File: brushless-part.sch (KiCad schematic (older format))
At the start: 13 parts, among them K1 Maxon-200142, K2 Maxon-200142, U2 DEC24/2, U3 DEC24/2

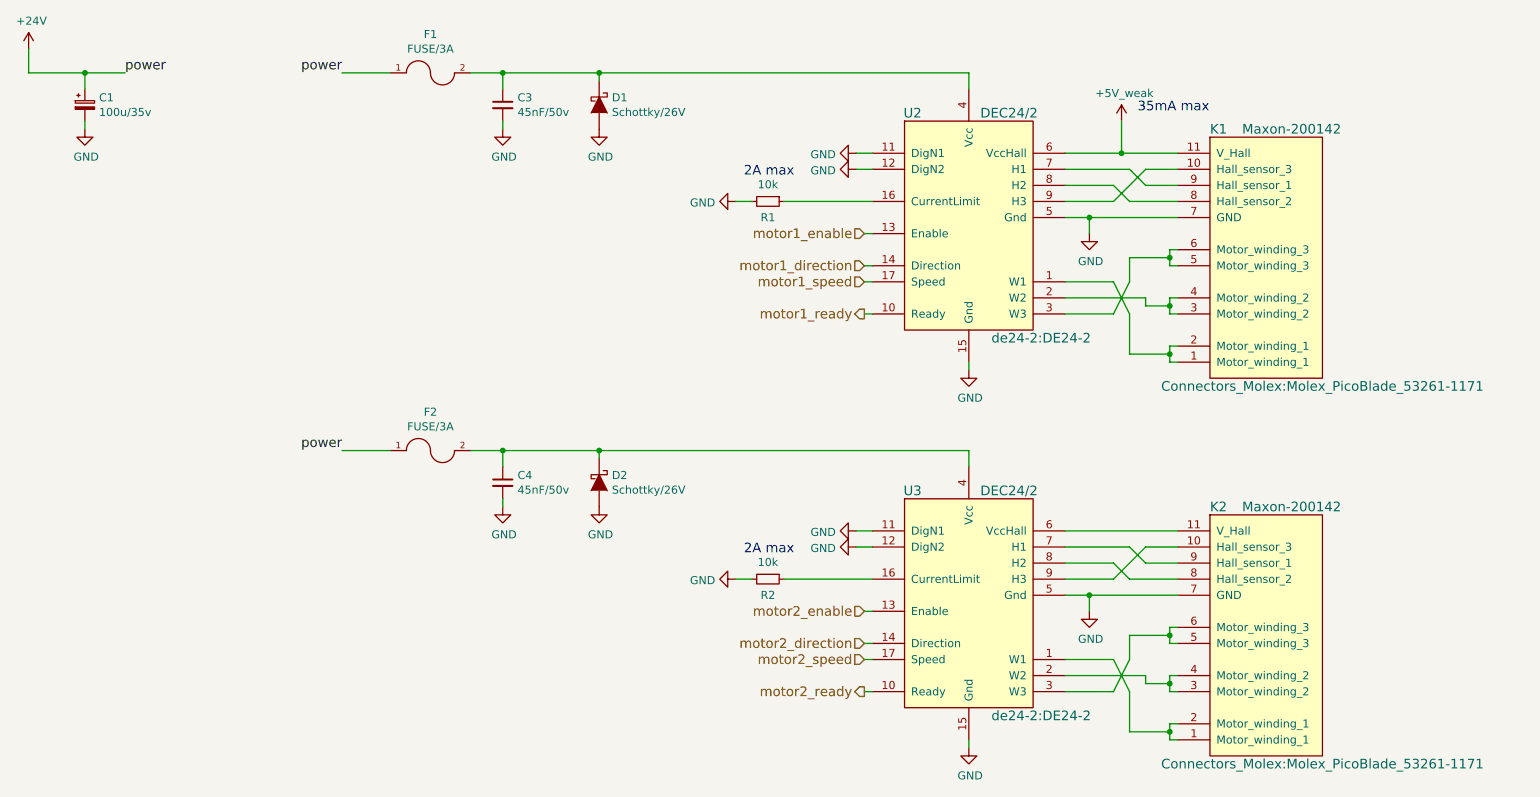
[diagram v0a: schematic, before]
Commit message: schematic seems ok, ongoing routing
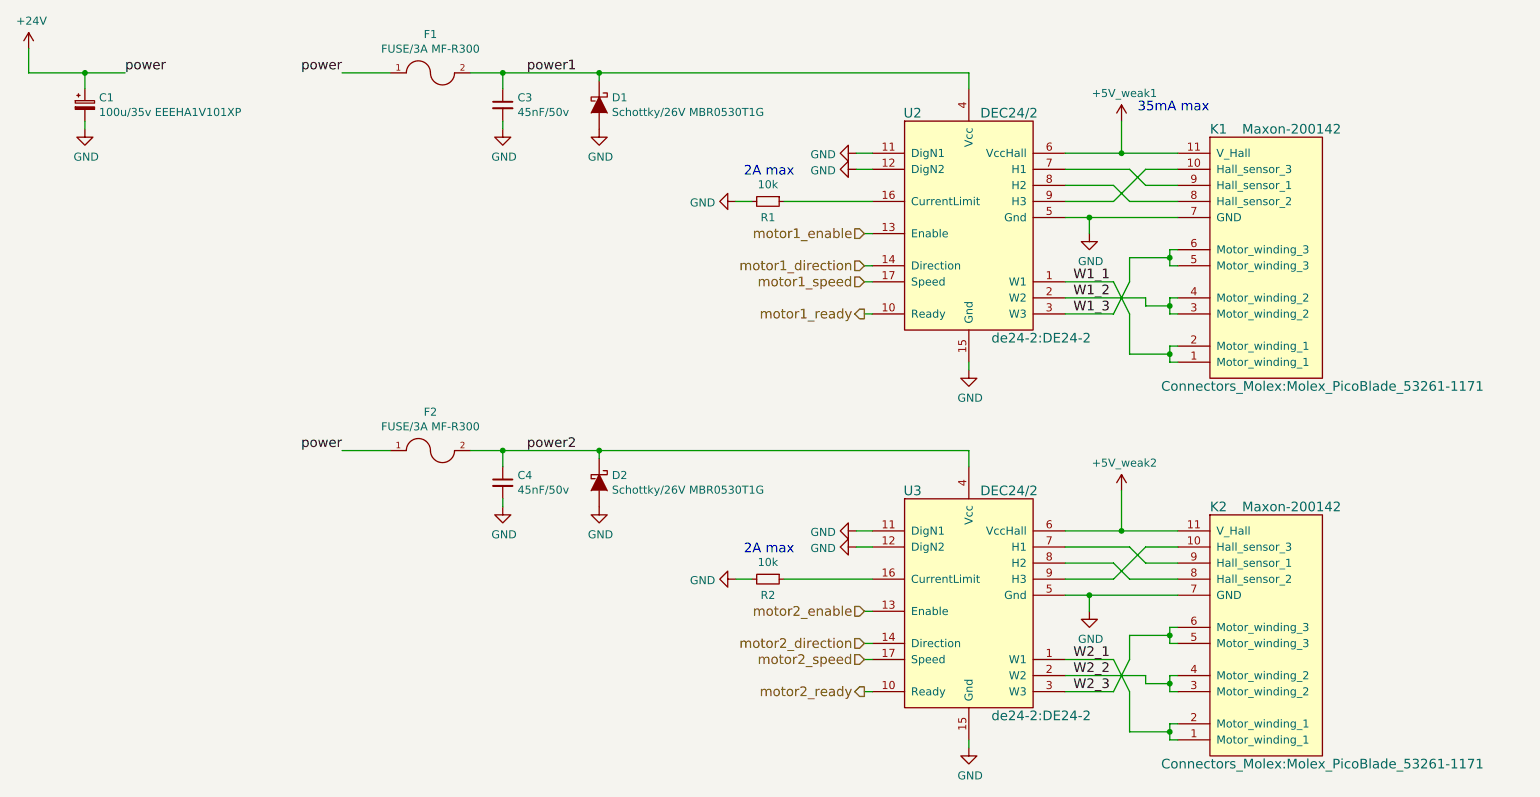
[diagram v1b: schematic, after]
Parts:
- C1: value 100u/35v -> 100u/35v EEEHA1V101XP; footprint Capacitors_ThroughHole:C_Radial_D10_L13_P5 -> Capacitors_SMD:c_elec_6.3x4.5
- C3, C4: footprint Capacitors_SMD:C_1210 -> Capacitors_SMD:C_0805
- D1, D2: value Schottky/26V -> Schottky/26V MBR0530T1G; footprint Diodes_SMD:DO-214AB -> Diodes_SMD:SOD-123
- F1: value FUSE/3A -> FUSE/3A MF-R300; footprint Fuse_Holders_and_Fuses:Fuse_SMD2920 -> Fuse_Holders_and_Fuses:Fuse_TE5_Littlefuse-395Series
- F2: value FUSE/3A -> FUSE/3A MF-R300
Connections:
- net W1_1: now reaches K1.1 (Motor_winding_1), K1.2 (Motor_winding_1), U2.1 (W1)
- net W1_2: now reaches K1.3 (Motor_winding_2), K1.4 (Motor_winding_2), U2.2 (W2)
- net W1_3: now reaches K1.5 (Motor_winding_3), K1.6 (Motor_winding_3), U2.3 (W3)
- net power1: now reaches C3.1, D1.1 (K), F1.2, U2.4 (Vcc)
- net W2_1: now reaches K2.1 (Motor_winding_1), K2.2 (Motor_winding_1), U3.1 (W1)
- net W2_2: now reaches K2.3 (Motor_winding_2), K2.4 (Motor_winding_2), U3.2 (W2)
- net W2_3: now reaches K2.5 (Motor_winding_3), K2.6 (Motor_winding_3), U3.3 (W3)
- net power2: now reaches C4.1, D2.1 (K), F2.2, U3.4 (Vcc)
- net +5V_weak2: now reaches K2.11 (V_Hall), U3.6 (VccHall)
- net +5V_weak renamed +5V_weak1
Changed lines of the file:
@@
 $Descr A4 11693 8268
 encoding utf-8
-Sheet 2 7
+Sheet 2 9
 Title "Brushless glue"
 Date "2016-04-02"
@@
 $EndComp
 $Comp
-L GND #PWR01
+L GND #PWR13
 U 1 1 570025FB
 P 7300 3700
-F 0 "#PWR01" H 7300 3450 50  0001 C CNN
+F 0 "#PWR13" H 7300 3450 50  0001 C CNN
 F 1 "GND" H 7308 3527 50  0000 C CNN
 F 2 "" H 7300 3700 50  0000 C CNN
@@
 $EndComp
 $Comp
-L GND #PWR02
+L GND #PWR15
 U 1 1 570025FD
 P 8050 2850
-F 0 "#PWR02" H 8050 2600 50  0001 C CNN
+F 0 "#PWR15" H 8050 2600 50  0001 C CNN
 F 1 "GND" H 8058 2677 50  0000 C CNN
 F 2 "" H 8050 2850 50  0000 C CNN
@@
 $EndComp
 $Comp
-L GND #PWR03
+L GND #PWR9
 U 1 1 570025FE
 P 6600 2350
-F 0 "#PWR03" H 6600 2100 50  0001 C CNN
+F 0 "#PWR9" H 6600 2100 50  0001 C CNN
 F 1 "GND" V 6608 2222 50  0000 R CNN
 F 2 "" H 6600 2350 50  0000 C CNN
@@
 $EndComp
 $Comp
-L GND #PWR04
+L GND #PWR10
 U 1 1 570025FF
 P 6600 2450
-F 0 "#PWR04" H 6600 2200 50  0001 C CNN
+F 0 "#PWR10" H 6600 2200 50  0001 C CNN
 F 1 "GND" V 6608 2322 50  0000 R CNN
 F 2 "" H 6600 2450 50  0000 C CNN
@@
 P 3950 1850
 F 0 "F1" H 3950 2090 50  0000 C CNN
-F 1 "FUSE/3A" H 3950 1999 50  0000 C CNN
-F 2 "Fuse_Holders_and_Fuses:Fuse_SMD2920" H 3950 1850 50  0001 C CNN
+F 1 "FUSE/3A MF-R300" H 3950 1999 50  0000 C CNN
+F 2 "Fuse_Holders_and_Fuses:Fuse_TE5_Littlefuse-395Series" H 3950 1850 50  0001 C CNN
 F 3 "" H 3950 1850 50  0000 C CNN
 	1    3950 1850
@@
 F 0 "C3" H 4492 2096 50  0000 L CNN
 F 1 "45nF/50v" H 4492 2005 50  0000 L CNN
-F 2 "Capacitors_SMD:C_1210" H 4400 2050 50  0001 C CNN
+F 2 "Capacitors_SMD:C_0805" H 4400 2050 50  0001 C CNN
 F 3 "" H 4400 2050 50  0000 C CNN
 	1    4400 2050
@@
 P 5000 2050
 F 0 "D1" V 4954 2129 50  0000 L CNN
-F 1 "Schottky/26V" V 5045 2129 50  0000 L CNN
-F 2 "Diodes_SMD:DO-214AB" H 5000 2050 50  0001 C CNN
-F 3 "" H 5000 2050 50  0000 C CNN
+F 1 "Schottky/26V MBR0530T1G" V 5045 2129 50  0000 L CNN
+F 2 "Diodes_SMD:SOD-123" H 5000 2050 50  0001 C CNN
+F 3 "http://www.farnell.com/datasheets/85890.pdf" H 5000 2050 50  0001 C CNN
 	1    5000 2050
 	0    1    1    0
 $EndComp
 $Comp
-L GND #PWR05
+L GND #PWR5
 U 1 1 57003EB2
 P 5000 2200
-F 0 "#PWR05" H 5000 1950 50  0001 C CNN
+F 0 "#PWR5" H 5000 1950 50  0001 C CNN
 F 1 "GND" H 5008 2027 50  0000 C CNN
 F 2 "" H 5000 2200 50  0000 C CNN
@@
 $EndComp
 $Comp
-L GND #PWR06
+L GND #PWR3
 U 1 1 57003EF1
 P 4400 2200
-F 0 "#PWR06" H 4400 1950 50  0001 C CNN
+F 0 "#PWR3" H 4400 1950 50  0001 C CNN
 F 1 "GND" H 4408 2027 50  0000 C CNN
 F 2 "" H 4400 2200 50  0000 C CNN
@@
 $EndComp
 $Comp
-L GND #PWR07
+L GND #PWR7
 U 1 1 570049DF
 P 5850 2650
-F 0 "#PWR07" H 5850 2400 50  0001 C CNN
+F 0 "#PWR7" H 5850 2400 50  0001 C CNN
 F 1 "GND" V 5858 2522 50  0000 R CNN
 F 2 "" H 5850 2650 50  0000 C CNN
@@
 $EndComp
 $Comp
-L GND #PWR08
+L GND #PWR14
 U 1 1 57005516
 P 7300 6050
-F 0 "#PWR08" H 7300 5800 50  0001 C CNN
+F 0 "#PWR14" H 7300 5800 50  0001 C CNN
 F 1 "GND" H 7308 5877 50  0000 C CNN
 F 2 "" H 7300 6050 50  0000 C CNN
@@
 $EndComp
 $Comp
-L GND #PWR09
+L GND #PWR16
 U 1 1 5700551D
 P 8050 5200
-F 0 "#PWR09" H 8050 4950 50  0001 C CNN
+F 0 "#PWR16" H 8050 4950 50  0001 C CNN
 F 1 "GND" H 8058 5027 50  0000 C CNN
 F 2 "" H 8050 5200 50  0000 C CNN
@@
 $EndComp
 $Comp
-L GND #PWR010
+L GND #PWR11
 U 1 1 57005525
 P 6600 4700
-F 0 "#PWR010" H 6600 4450 50  0001 C CNN
+F 0 "#PWR11" H 6600 4450 50  0001 C CNN
 F 1 "GND" V 6608 4572 50  0000 R CNN
 F 2 "" H 6600 4700 50  0000 C CNN
@@
 $EndComp
 $Comp
-L GND #PWR011
+L GND #PWR12
 U 1 1 5700552B
 P 6600 4800
-F 0 "#PWR011" H 6600 4550 50  0001 C CNN
+F 0 "#PWR12" H 6600 4550 50  0001 C CNN
 F 1 "GND" V 6608 4672 50  0000 R CNN
 F 2 "" H 6600 4800 50  0000 C CNN
@@
 $EndComp
 $Comp
-L GND #PWR012
+L GND #PWR8
 U 1 1 5700554F
 P 5850 5000
-F 0 "#PWR012" H 5850 4750 50  0001 C CNN
+F 0 "#PWR8" H 5850 4750 50  0001 C CNN
 F 1 "GND" V 5858 4872 50  0000 R CNN
 F 2 "" H 5850 5000 50  0000 C CNN
@@
 P 1800 2050
 F 0 "C1" H 1888 2096 50  0000 L CNN
-F 1 "100u/35v" H 1888 2005 50  0000 L CNN
-F 2 "Capacitors_ThroughHole:C_Radial_D10_L13_P5" H 1800 2050 50  0001 C CNN
+F 1 "100u/35v EEEHA1V101XP" H 1888 2005 50  0000 L CNN
+F 2 "Capacitors_SMD:c_elec_6.3x4.5" H 1800 2050 50  0001 C CNN
 F 3 "" H 1800 2050 50  0000 C CNN
 	1    1800 2050
@@
 $EndComp
 $Comp
-L GND #PWR013
+L GND #PWR2
 U 1 1 57005F05
 P 1800 2200
-F 0 "#PWR013" H 1800 1950 50  0001 C CNN
+F 0 "#PWR2" H 1800 1950 50  0001 C CNN
 F 1 "GND" H 1808 2027 50  0000 C CNN
 F 2 "" H 1800 2200 50  0000 C CNN
@@
 P 3950 4200
 F 0 "F2" H 3950 4440 50  0000 C CNN
-F 1 "FUSE/3A" H 3950 4349 50  0000 C CNN
+F 1 "FUSE/3A MF-R300" H 3950 4349 50  0000 C CNN
 F 2 "Fuse_Holders_and_Fuses:Fuse_TE5_Littlefuse-395Series" H 3950 4200 50  0001 C CNN
 F 3 "" H 3950 4200 50  0000 C CNN
@@
 F 0 "C4" H 4492 4446 50  0000 L CNN
 F 1 "45nF/50v" H 4492 4355 50  0000 L CNN
-F 2 "Capacitors_SMD:C_1210" H 4400 4400 50  0001 C CNN
+F 2 "Capacitors_SMD:C_0805" H 4400 4400 50  0001 C CNN
 F 3 "" H 4400 4400 50  0000 C CNN
 	1    4400 4400
@@
 P 5000 4400
 F 0 "D2" V 4954 4479 50  0000 L CNN
-F 1 "Schottky/26V" V 5045 4479 50  0000 L CNN
-F 2 "Diodes_SMD:DO-214AB" H 5000 4400 50  0001 C CNN
-F 3 "" H 5000 4400 50  0000 C CNN
+F 1 "Schottky/26V MBR0530T1G" V 5045 4479 50  0000 L CNN
+F 2 "Diodes_SMD:SOD-123" H 5000 4400 50  0001 C CNN
+F 3 "http://www.farnell.com/datasheets/85890.pdf" H 5000 4400 50  0001 C CNN
 	1    5000 4400
 	0    1    1    0
 $EndComp
 $Comp
-L GND #PWR014
+L GND #PWR6
 U 1 1 570062E1
 P 5000 4550
-F 0 "#PWR014" H 5000 4300 50  0001 C CNN
+F 0 "#PWR6" H 5000 4300 50  0001 C CNN
 F 1 "GND" H 5008 4377 50  0000 C CNN
 F 2 "" H 5000 4550 50  0000 C CNN
@@
 $EndComp
 $Comp
-L GND #PWR015
+L GND #PWR4
 U 1 1 570062E7
 P 4400 4550
-F 0 "#PWR015" H 4400 4300 50  0001 C CNN
+F 0 "#PWR4" H 4400 4300 50  0001 C CNN
 F 1 "GND" H 4408 4377 50  0000 C CNN
 F 2 "" H 4400 4550 50  0000 C CNN
@@
 	1450 1850 2050 1850
 $Comp
-L +24V #PWR016
+L +24V #PWR1
 U 1 1 5707C03C
 P 1450 1700
-F 0 "#PWR016" H 1450 1550 50  0001 C CNN
+F 0 "#PWR1" H 1450 1550 50  0001 C CNN
 F 1 "+24V" H 1468 1873 50  0000 C CNN
 F 2 "" H 1450 1700 50  0000 C CNN
@@
 Wire Wire Line
 	1450 1850 1450 1700
-$Comp
-L +5V_weak #PWR017
-U 1 1 5704F3C7
-P 8250 2150
-F 0 "#PWR017" H 8250 2000 50  0001 C CNN
-F 1 "+5V_weak" H 8268 2323 50  0000 C CNN
-F 2 "" H 8250 2150 50  0000 C CNN
-F 3 "" H 8250 2150 50  0000 C CNN
-	1    8250 2150
-	1    0    0    -1
-$EndComp
 Wire Wire Line
 	8250 2350 8250 2150
@@
 Wire Wire Line
 	7300 1850 7300 1950
+Text Label 7950 3150 0    60   ~ 0
+W1_1
+Text Label 7950 3250 0    60   ~ 0
+W1_2
+Text Label 7950 3350 0    60   ~ 0
+W1_3
+Text Label 7950 5500 0    60   ~ 0
+W2_1
+Text Label 7950 5600 0    60   ~ 0
+W2_2
+Text Label 7950 5700 0    60   ~ 0
+W2_3
+Text Label 4550 1850 0    60   ~ 0
+power1
+Text Label 4550 4200 0    60   ~ 0
+power2
+$Comp
+L +5V_weak1 #PWR?
+U 1 1 5706CC78
+P 8250 2150
+F 0 "#PWR?" H 8250 2000 50  0001 C CNN
+F 1 "+5V_weak1" H 8268 2323 50  0000 C CNN
+F 2 "" H 8250 2150 50  0000 C CNN
+F 3 "" H 8250 2150 50  0000 C CNN
+	1    8250 2150
+	1    0    0    -1
+$EndComp
+$Comp
+L +5V_weak2 #PWR?
+U 1 1 5706CE60
+P 8250 4450
+F 0 "#PWR?" H 8250 4300 50  0001 C CNN
+F 1 "+5V_weak2" H 8268 4623 50  0000 C CNN
+F 2 "" H 8250 4450 50  0000 C CNN
+F 3 "" H 8250 4450 50  0000 C CNN
+	1    8250 4450
+	1    0    0    -1
+$EndComp
+Wire Wire Line
+	8250 4450 8250 4700
+Connection ~ 8250 4700
 $EndSCHEMATC
